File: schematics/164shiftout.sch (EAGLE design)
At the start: 3 parts, among them IC5 74HC164N

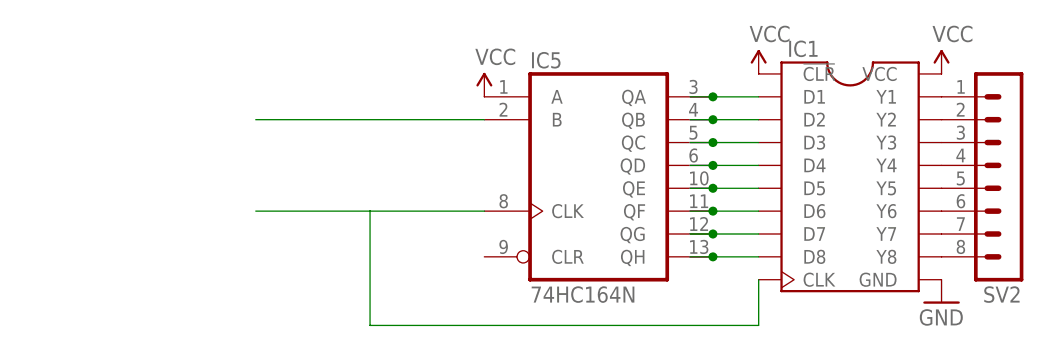
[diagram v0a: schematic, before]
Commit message: rework the schematics for cnc milling
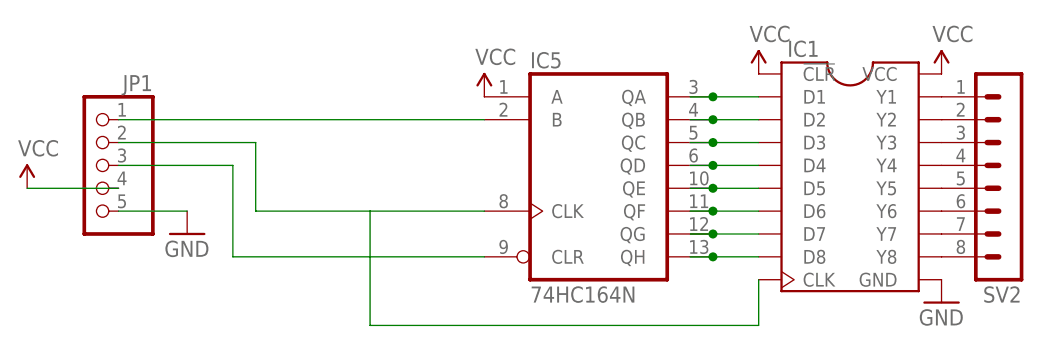
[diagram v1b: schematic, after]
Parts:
- added JP1: (no value), pinhead:PINHD-1X55X2MM
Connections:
- new net N$1: IC5A.CLR, JP1.3
- net GND: now also JP1.5
- net N$59: now also JP1.1
- net N$60: now also JP1.2
- net VCC: now also JP1.4
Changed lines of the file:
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@@
 <part name="IC5" library="74xx-us" deviceset="74*164" device="N" technology="HC"/>
 <part name="SUPPLY8" library="SparkFun-Aesthetics" deviceset="VCC" device=""/>
+<part name="JP1" library="pinhead" deviceset="PINHD-1X5" device="5X2MM"/>
+<part name="GND1" library="SparkFun-Aesthetics" deviceset="GND" device=""/>
+<part name="SUPPLY1" library="SparkFun-Aesthetics" deviceset="VCC" device=""/>
 </parts>
 <sheets>
@@
 <instance part="IC5" gate="A" x="160.02" y="114.3"/>
 <instance part="SUPPLY8" gate="1" x="147.32" y="121.92"/>
+<instance part="JP1" gate="A" x="104.14" y="114.3" rot="MR0"/>
+<instance part="GND1" gate="1" x="114.3" y="106.68"/>
+<instance part="SUPPLY1" gate="1" x="96.52" y="111.76"/>
 </instances>
 <busses>
@@
 <pinref part="GND14" gate="1" pin="GND"/>
 </segment>
+<segment>
+<pinref part="JP1" gate="A" pin="5"/>
+<pinref part="GND1" gate="1" pin="GND"/>
+<wire x1="114.3" y1="109.22" x2="106.68" y2="109.22" width="0.1524" layer="91"/>
+</segment>
 </net>
 <net name="VCC" class="0">
@@
 <pinref part="IC5" gate="A" pin="A"/>
 <pinref part="SUPPLY8" gate="1" pin="VCC"/>
+</segment>
+<segment>
+<pinref part="SUPPLY1" gate="1" pin="VCC"/>
+<pinref part="JP1" gate="A" pin="4"/>
+<wire x1="96.52" y1="111.76" x2="106.68" y2="111.76" width="0.1524" layer="91"/>
 </segment>
 </net>
@@
 <wire x1="177.8" y1="96.52" x2="177.8" y2="101.6" width="0.1524" layer="91"/>
 <wire x1="134.62" y1="109.22" x2="121.92" y2="109.22" width="0.1524" layer="91"/>
+<wire x1="121.92" y1="109.22" x2="121.92" y2="116.84" width="0.1524" layer="91"/>
+<pinref part="JP1" gate="A" pin="2"/>
+<wire x1="121.92" y1="116.84" x2="106.68" y2="116.84" width="0.1524" layer="91"/>
 </segment>
 </net>
@@
 <segment>
 <pinref part="IC5" gate="A" pin="B"/>
-<wire x1="121.92" y1="119.38" x2="147.32" y2="119.38" width="0.1524" layer="91"/>
-</segment>
-</net>
+<wire x1="106.68" y1="119.38" x2="147.32" y2="119.38" width="0.1524" layer="91"/>
+<pinref part="JP1" gate="A" pin="1"/>
+</segment>
+</net>
+<net name="N$1" class="0">
+<segment>
+<pinref part="IC5" gate="A" pin="CLR"/>
+<wire x1="147.32" y1="104.14" x2="119.38" y2="104.14" width="0.1524" layer="91"/>
+<wire x1="119.38" y1="104.14" x2="119.38" y2="114.3" width="0.1524" layer="91"/>
+<pinref part="JP1" gate="A" pin="3"/>
+<wire x1="119.38" y1="114.3" x2="106.68" y2="114.3" width="0.1524" layer="91"/>
+</segment>
+</net>
